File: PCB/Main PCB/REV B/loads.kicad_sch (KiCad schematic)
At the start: 11 parts

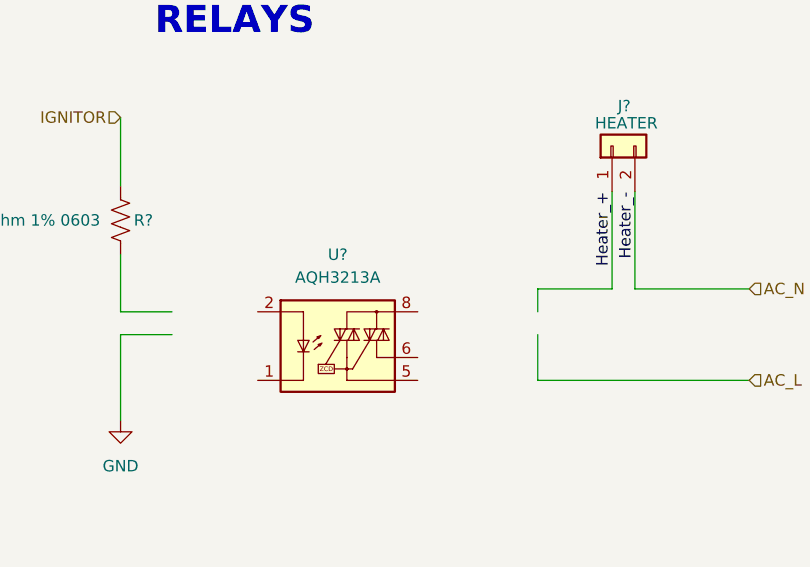
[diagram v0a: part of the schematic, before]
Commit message: Component changes, new ignitor relay - need to do supporting circuity
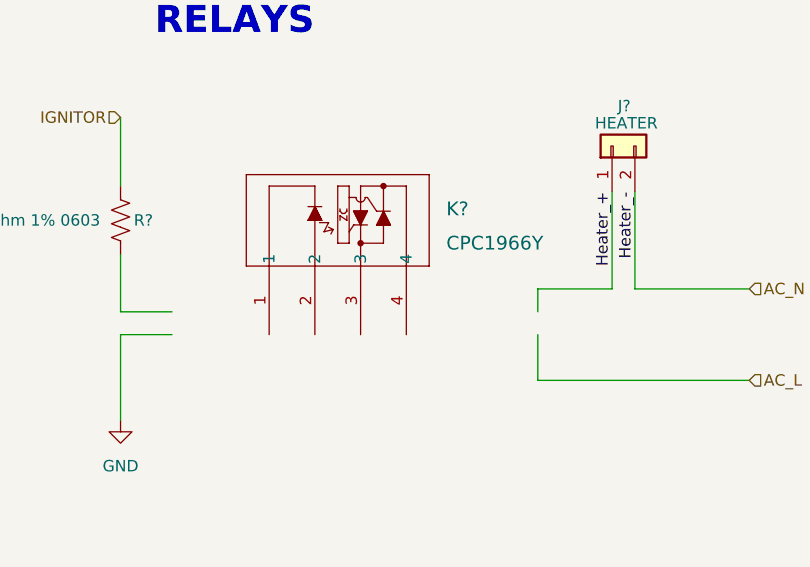
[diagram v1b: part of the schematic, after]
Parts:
- removed U?: AQH3213A, Package_SO:SSO-7-8_6.4x9.78mm_P2.54mm, symbol Relay_SolidState:AQH3213A
- added K?: CPC1966Y, Customs Smoker:SIP4_CPC1966Y_LTF, symbol CPC1966Y:CPC1966Y
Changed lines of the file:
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@@
     (pin "2")
-  )
-  (symbol (lib_id "Relay_SolidState:AQH3213A") (at 110.49 73.66 0) (unit 1)
-    (in_bom yes) (on_board yes) (fields_autoplaced)
-    (property "Reference" "U?" (id 0) (at 109.22 64.77 0))
-    (property "Value" "AQH3213A" (id 1) (at 109.22 67.31 0))
-    (property "Footprint" "Package_SO:SSO-7-8_6.4x9.78mm_P2.54mm" (id 2) (at 105.41 68.58 0)
-      (effects (font (size 1.27 1.27) italic) (justify left) hide)
-    )
-    (property "Datasheet" "https://b2b-api.panasonic.eu/file_stream/pids/fileversion/2787" (id 3) (at 107.95 73.66 0)
-      (effects (font (size 1.27 1.27)) (justify left) hide)
-    )
-    (property "Manufacturer" "Panasonic Electric Works" (id 4) (at 110.49 73.66 0)
-      (effects (font (size 1.27 1.27)) hide)
-    )
-    (property "Manufacturer Part Number" "AQH3213AX" (id 5) (at 110.49 73.66 0)
-      (effects (font (size 1.27 1.27)) hide)
-    )
-    (property "Vendor" "Digikey" (id 6) (at 110.49 73.66 0)
-      (effects (font (size 1.27 1.27)) hide)
-    )
-    (property "Vendor Part Number" "255-6001-1-ND" (id 7) (at 110.49 73.66 0)
-      (effects (font (size 1.27 1.27)) hide)
-    )
-    (pin "1")
-    (pin "2")
-    (pin "3")
-    (pin "4")
-    (pin "5")
-    (pin "6")
-    (pin "8")
   )
   (symbol (lib_id "power:GND") (at 84.455 185.42 0) (mirror y) (unit 1)
@@
     (pin "8")
   )
+  (symbol (lib_id "CPC1966Y:CPC1966Y") (at 101.6 73.66 90) (unit 1)
+    (in_bom yes) (on_board yes) (fields_autoplaced)
+    (property "Reference" "K?" (id 0) (at 121.285 59.69 90)
+      (effects (font (size 1.524 1.524)) (justify right))
+    )
+    (property "Value" "CPC1966Y" (id 1) (at 121.285 63.5 90)
+      (effects (font (size 1.524 1.524)) (justify right))
+    )
+    (property "Footprint" "Customs Smoker:SIP4_CPC1966Y_LTF" (id 2) (at 101.6 73.66 0)
+      (effects (font (size 1.27 1.27) italic) hide)
+    )
+    (property "Datasheet" "CPC1966Y" (id 3) (at 101.6 73.66 0)
+      (effects (font (size 1.27 1.27) italic) hide)
+    )
+    (property "Manufacturer" "IXYS Integrated Circuits Division" (id 4) (at 101.6 73.66 0)
+      (effects (font (size 1.27 1.27)) hide)
+    )
+    (property "Manufacturer Part Number" "CPC1966Y" (id 5) (at 101.6 73.66 0)
+      (effects (font (size 1.27 1.27)) hide)
+    )
+    (property "Vendor" "Digikey" (id 6) (at 101.6 73.66 0)
+      (effects (font (size 1.27 1.27)) hide)
+    )
+    (property "Vendor Part Number" "CLA393-ND" (id 7) (at 101.6 73.66 0)
+      (effects (font (size 1.27 1.27)) hide)
+    )
+    (pin "1")
+    (pin "2")
+    (pin "3")
+    (pin "4")
+  )
   (symbol (lib_id "power:GND") (at 84.455 138.43 0) (mirror y) (unit 1)

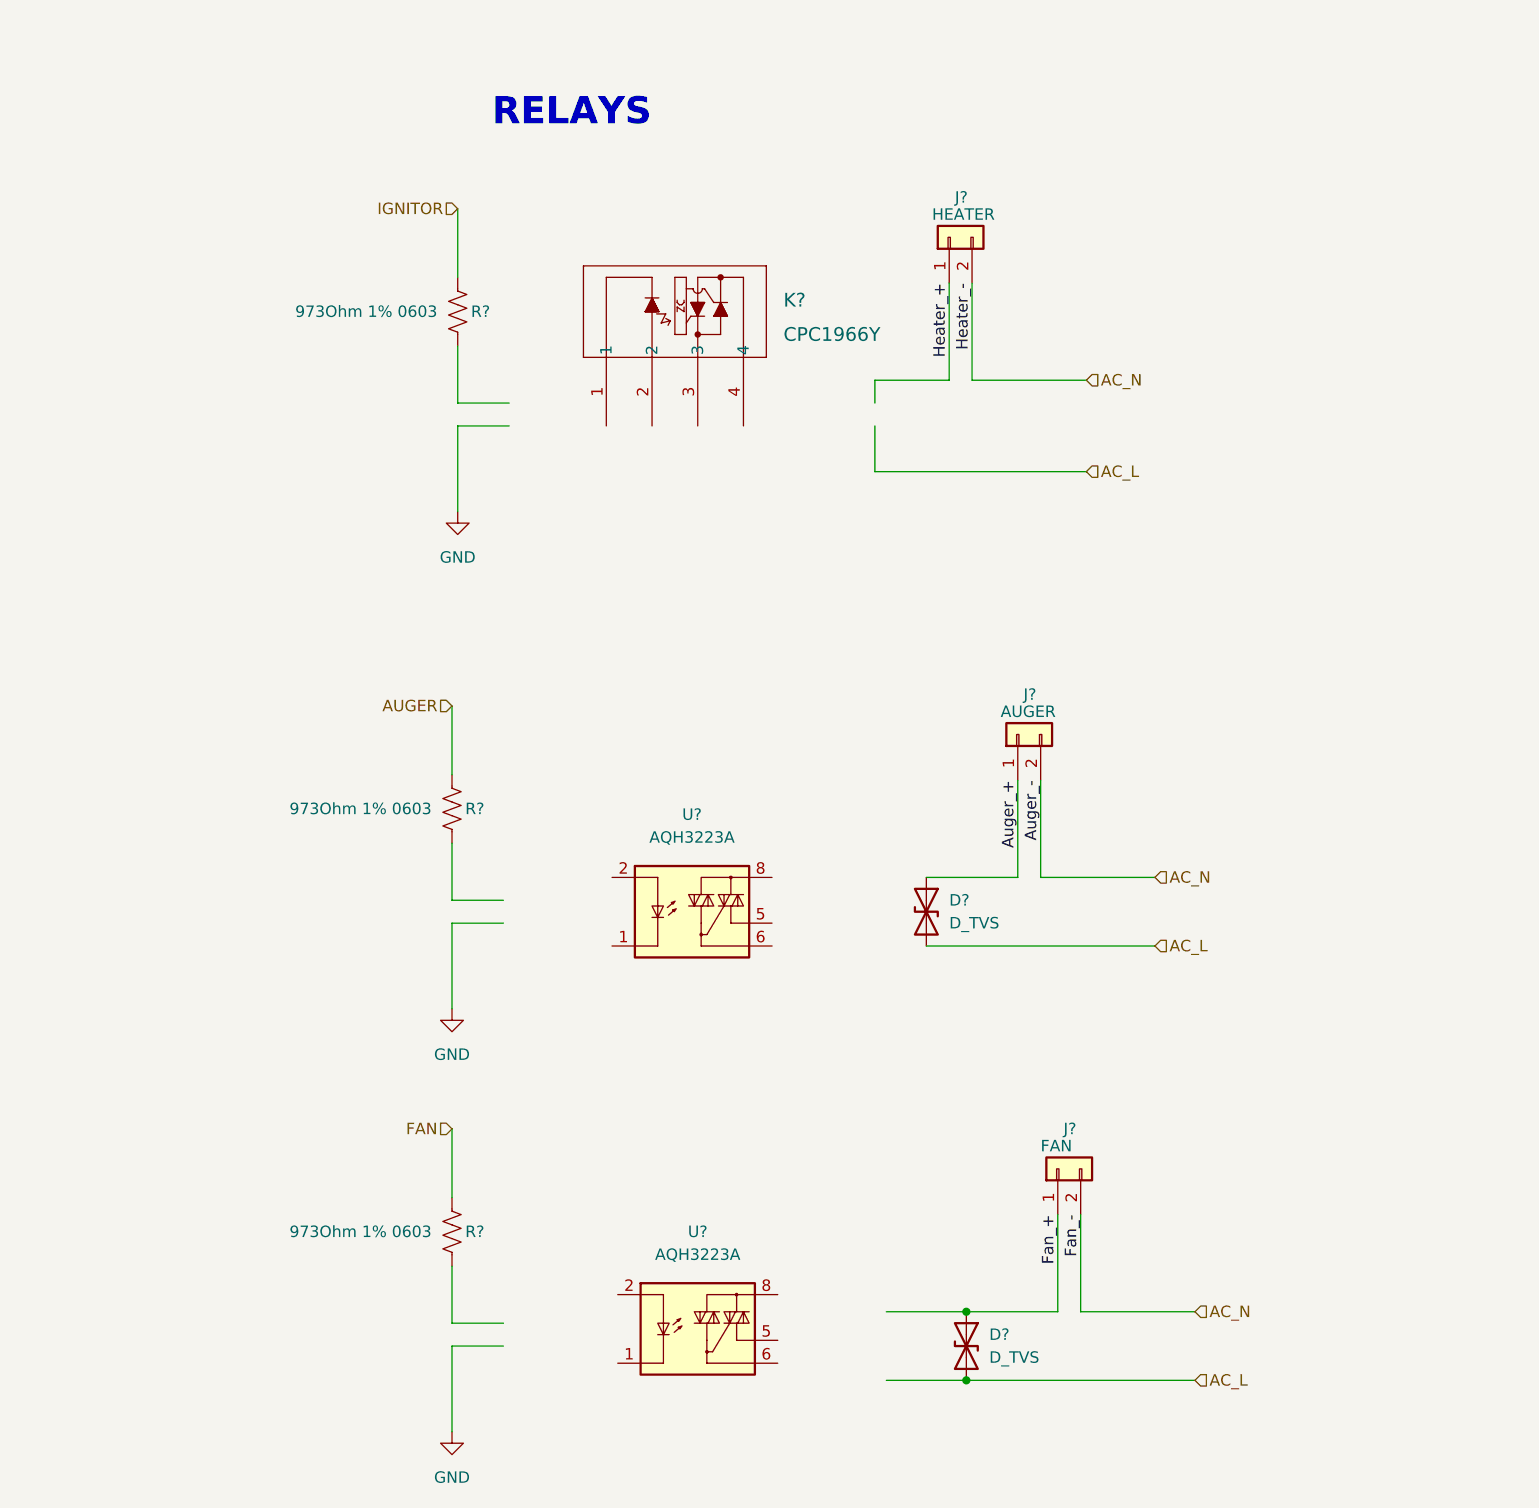
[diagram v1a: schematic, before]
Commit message: Relay circuitry complete - snubber added to inductive loads
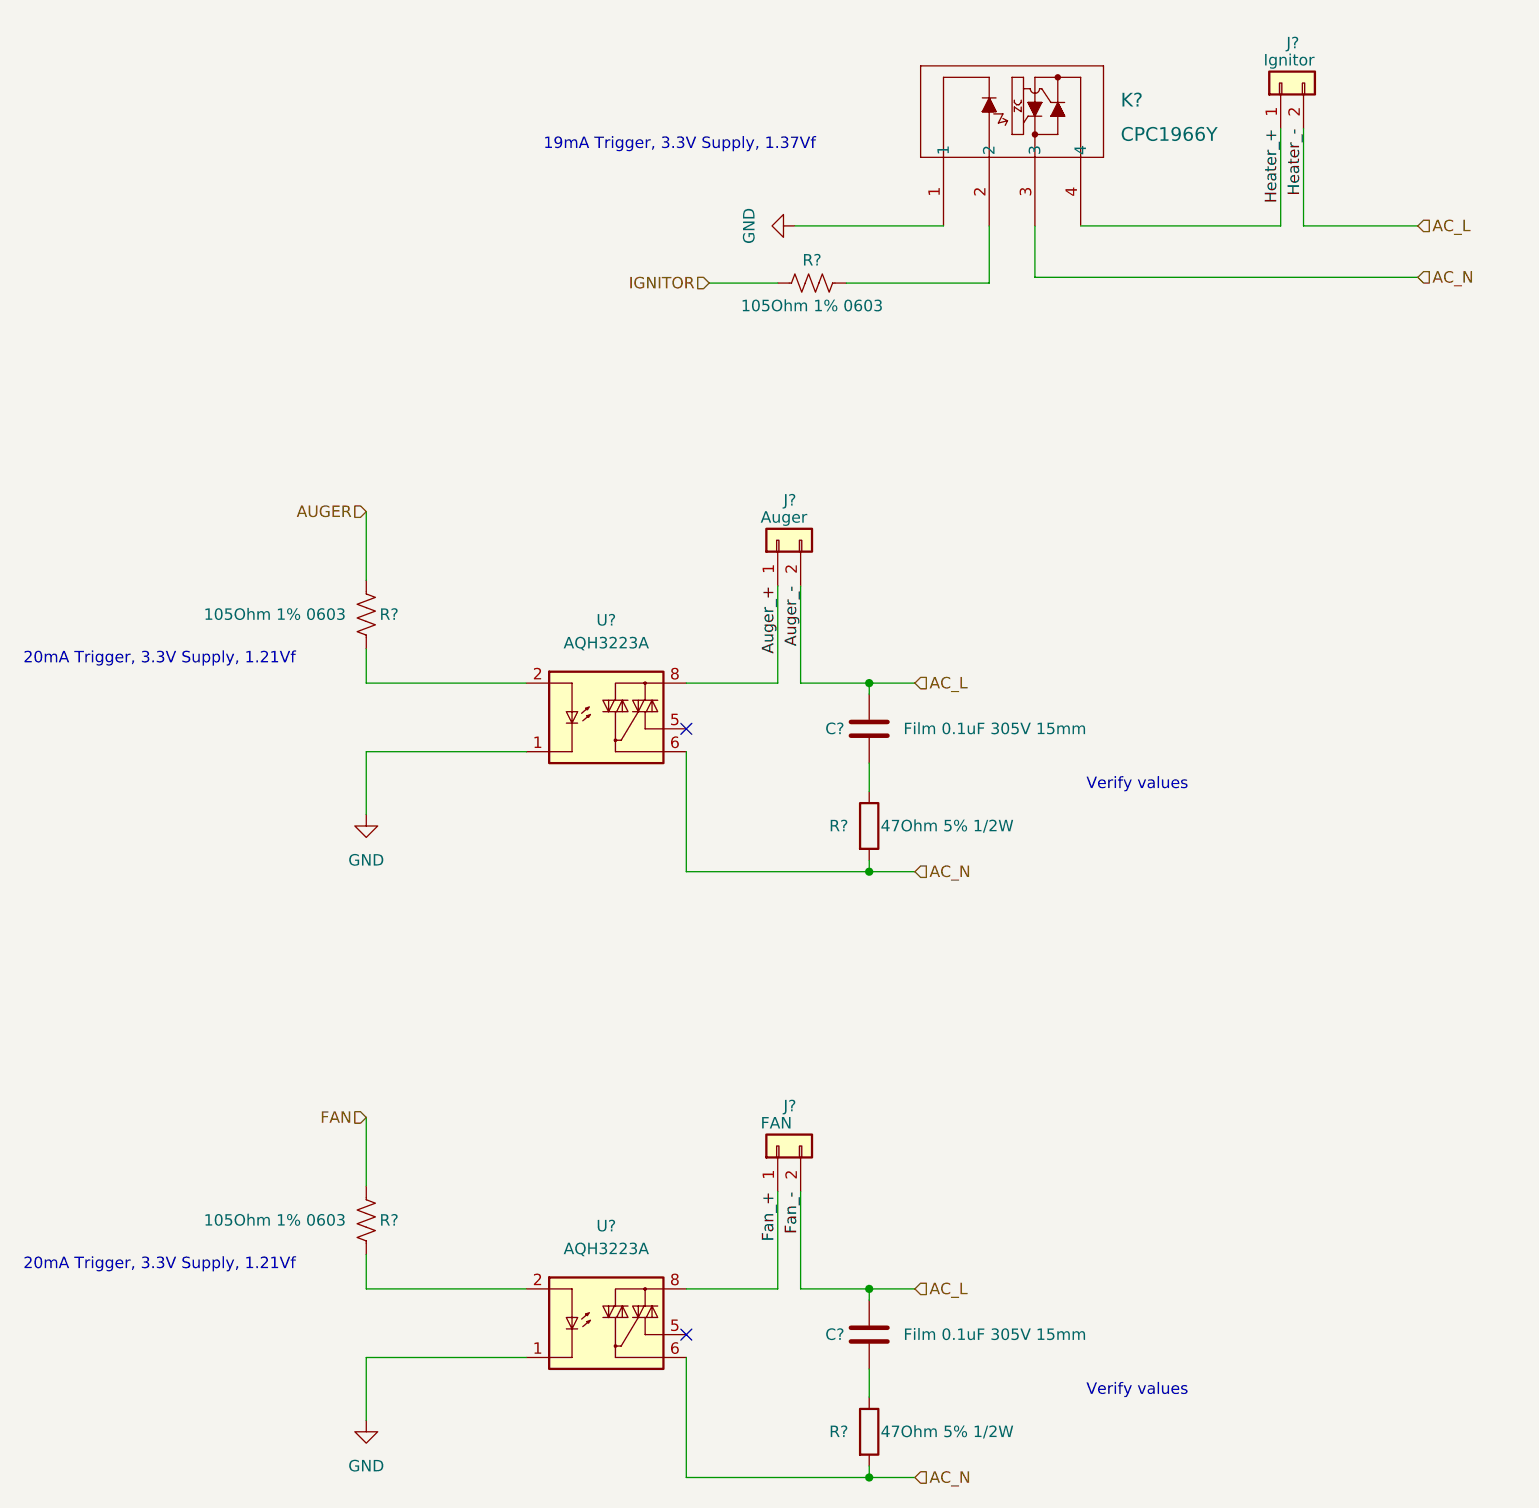
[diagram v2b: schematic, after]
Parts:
- removed D? (x2): D_TVS, Customs Smoker:DIOM7959X262N, symbol Device:D_TVS
- removed R? (x2): 973Ohm 1% 0603, Resistor_SMD:R_0603_1608Metric, symbol Device:R_US
- removed U?: AQH3223A, Package_SO:SSO-7-8_6.4x9.78mm_P2.54mm, symbol Relay_SolidState:AQH3223A
- added C? (x2): Film 0.1uF 305V 15mm, Capacitor_THT:C_Rect_L18.0mm_W6.0mm_P15.00mm_FKS3_FKP3, symbol Device:C
- added R? (x2): 47Ohm 5% 1/2W, Resistor_THT:R_Axial_DIN0204_L3.6mm_D1.6mm_P5.08mm_Vertical, symbol Device:R
- added R? (x2): 105Ohm 1% 0603, Resistor_SMD:R_0603_1608Metric, symbol Device:R_US
- added U?: AQH3223A, Package_SO:SSO-7-8_6.4x9.78mm_P2.54mm, symbol Relay_SolidState:AQH3223A
- J?: value HEATER -> Ignitor
- J?: value AUGER -> Auger
- R?: value 973Ohm 1% 0603 -> 105Ohm 1% 0603; Manufacturer Part Number RC0603FR-07976RL -> RC0603FR-07105RL; Vendor Part Number 311-976HRCT-ND -> 311-105HRCT-ND
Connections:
- net AC_L: now also J?.2 (Pin_2), J?.2 (Pin_2), J?.2 (Pin_2), C?.1, C?.1
- net AC_N: now also K?.3, U?.6, R?.2, R?.2, U?.6; no longer J?.2 (Pin_2), J?.2 (Pin_2), J?.2 (Pin_2)
- net Auger_+: now also U?.8
- net FAN: now also R?.1
- net Fan_+: now also U?.8
- net GND: now also K?.1, U?.1, U?.3, U?.4, U?.1, U?.3, U?.4
- net Heater_+: now also K?.4
- net IGNITOR: now also R?.1
- net at U?.2: now also R?.2
- net at K?.2: now also R?.2
- new net: R?.2, U?.2
- new net: C?.2, R?.1 (x2)
- no-connect marks 0 -> 2
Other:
- note added: "19mA Trigger, 3.3V Supply, 1.37Vf"
- note added: "20mA Trigger, 3.3V Supply, 1.21Vf"
- note added: "Verify values"
- note removed: "RELAYS"
- moved on the sheet: J?, K?, R?, U?
